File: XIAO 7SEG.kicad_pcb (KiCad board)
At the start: 2 copper layers, 21.1 x 17.8 mm, 8 parts, among them J2 DNP, J4 DNP, Q1 AO3400A, Q2 AO3400A, U1 GS2816CW-G, U2 GS2816CW-G

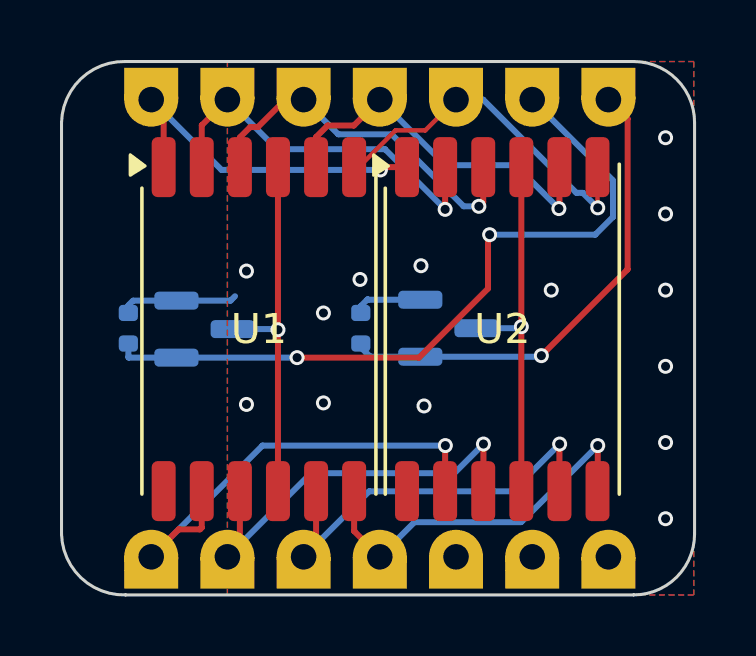
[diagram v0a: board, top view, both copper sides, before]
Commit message: Increase min track/gap to 0.154mm
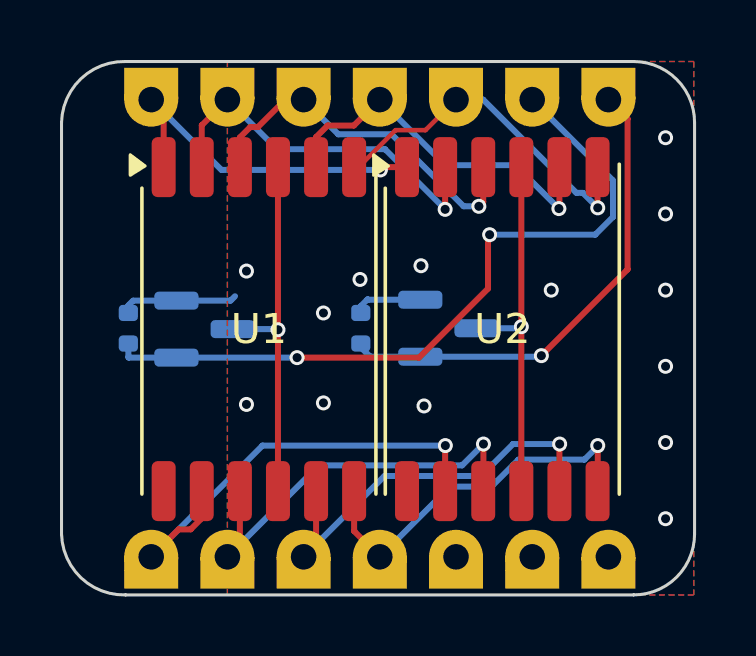
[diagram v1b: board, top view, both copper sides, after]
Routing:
- net SDA: track 12.3 -> 11.7 mm
- net SCK: track 14.0 -> 13.4 mm
- net MISO: track 14.0 -> 13.4 mm
- net TX: track 12.0 -> 11.4 mm
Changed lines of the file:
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@@
 		(title "Xiao_7Seg")
 		(date "2025-08-24")
-		(rev "1")
+		(rev "1.1")
 	)
 	(layers
@@
 	)
 	(segment
-		(start 144.145 109.73)
-		(end 144.145 109.855)
-		(width 0.2)
-		(layer "B.Cu")
-		(net 3)
-	)
-	(segment
 		(start 144.4904 110.17)
 		(end 146.1285 110.17)
@@
 	)
 	(segment
-		(start 142.0368 110.1852)
-		(end 142.022 110.2)
-		(width 0.2)
-		(layer "B.Cu")
-		(net 4)
-	)
-	(segment
 		(start 149.86 101.6)
 		(end 152.5524 104.2924)
@@
 	)
 	(segment
-		(start 145.305502 102.624)
-		(end 146.296 102.624)
-		(width 0.15)
-		(layer "F.Cu")
-		(net 5)
-	)
-	(segment
-		(start 144.079502 103.85)
-		(end 145.305502 102.624)
-		(width 0.15)
+		(start 143.925 103.85)
+		(end 144.071018 103.85)
+		(width 0.154)
 		(layer "F.Cu")
 		(net 5)
 	)
 	(segment
-		(start 143.925 103.85)
-		(end 144.079502 103.85)
-		(width 0.15)
+		(start 144.071018 103.85)
+		(end 145.303018 102.618)
+		(width 0.154)
 		(layer "F.Cu")
 		(net 5)
@@
 		(start 152.0375 103.85)
 		(end 152.0375 105.1999)
-		(width 0.15)
+		(width 0.2)
 		(layer "F.Cu")
 		(net 5)
 	)
 	(segment
-		(start 152.0375 105.1999)
-		(end 152.0444 105.2068)
-		(width 0.15)
+		(start 146.302 102.618)
+		(end 147.32 101.6)
+		(width 0.154)
 		(layer "F.Cu")
 		(net 5)
 	)
 	(segment
-		(start 146.296 102.624)
-		(end 147.32 101.6)
-		(width 0.15)
+		(start 145.303018 102.618)
+		(end 146.302 102.618)
+		(width 0.154)
 		(layer "F.Cu")
 		(net 5)
@@
 	)
 	(segment
-		(start 142.24 101.6)
-		(end 141.6304 101.6)
-		(width 0.2)
-		(layer "F.Cu")
-		(net 6)
-	)
-	(segment
 		(start 140.716 102.5144)
 		(end 140.462 102.5144)
@@
 	)
 	(segment
-		(start 152.0444 114.6431)
-		(end 152.0375 114.65)
-		(width 0.2)
-		(layer "F.Cu")
-		(net 8)
-	)
-	(segment
 		(start 143.925 115.985)
 		(end 144.78 116.84)
@@
 	)
 	(segment
-		(start 144.78 116.84)
-		(end 145.936 115.684)
+		(start 148.5 114.5)
+		(end 149.4 113.6)
+		(width 0.2)
+		(layer "B.Cu")
+		(net 8)
+	)
+	(segment
+		(start 151.6 113.6)
+		(end 152.0444 113.1556)
+		(width 0.2)
+		(layer "B.Cu")
+		(net 8)
+	)
+	(segment
+		(start 147.12 114.5)
+		(end 148.5 114.5)
 		(width 0.2)
 		(layer "B.Cu")
@@
 	)
 	(segment
-		(start 145.936 115.684)
-		(end 149.492 115.684)
+		(start 149.4 113.6)
+		(end 151.6 113.6)
 		(width 0.2)
 		(layer "B.Cu")
@@
 	)
 	(segment
-		(start 149.492 115.684)
+		(start 144.78 116.84)
+		(end 147.12 114.5)
+		(width 0.2)
+		(layer "B.Cu")
+		(net 8)
+	)
+	(segment
+		(start 152.0444 113.1556)
 		(end 152.0444 113.1316)
 		(width 0.2)
@@
 	)
 	(segment
-		(start 137.575 102.015)
-		(end 137.16 101.6)
-		(width 0.2)
-		(layer "F.Cu")
-		(net 10)
-	)
-	(segment
 		(start 137.575 103.85)
 		(end 137.575 102.015)
@@
 	)
 	(segment
-		(start 138.845 115.8662)
-		(end 138.845 114.65)
+		(start 138.4744 115.9256)
+		(end 138.845 115.555)
 		(width 0.2)
 		(layer "F.Cu")
@@
 	)
 	(segment
-		(start 138.7856 115.9256)
-		(end 138.845 115.8662)
+		(start 138.845 115.555)
+		(end 138.845 114.65)
 		(width 0.2)
 		(layer "F.Cu")
@@
 	(segment
 		(start 138.0744 115.9256)
-		(end 138.7856 115.9256)
+		(end 138.4744 115.9256)
 		(width 0.2)
 		(layer "F.Cu")
@@
 		(net 12)
 	)
-	(segment
-		(start 148.2344 114.6431)
-		(end 148.2275 114.65)
-		(width 0.2)
-		(layer "F.Cu")
-		(net 12)
-	)
-	(segment
-		(start 139.7 116.84)
-		(end 140.115 116.425)
-		(width 0.2)
-		(layer "F.Cu")
-		(net 12)
-	)
 	(via
 		(at 148.2344 113.0808)
@@
 	)
 	(segment
-		(start 142.4884 114.0516)
-		(end 147.2636 114.0516)
+		(start 147.5232 113.792)
+		(end 148.2344 113.0808)
 		(width 0.2)
 		(layer "B.Cu")
@@
 	)
 	(segment
-		(start 139.7 116.84)
-		(end 142.4884 114.0516)
+		(start 142.748 113.792)
+		(end 147.5232 113.792)
 		(width 0.2)
 		(layer "B.Cu")
@@
 	)
 	(segment
-		(start 147.2636 114.0516)
-		(end 148.2344 113.0808)
+		(start 139.7 116.84)
+		(end 142.748 113.792)
 		(width 0.2)
 		(layer "B.Cu")
@@
 	)
 	(segment
-		(start 142.24 116.84)
-		(end 142.655 116.425)
-		(width 0.2)
-		(layer "F.Cu")
-		(net 13)
-	)
-	(segment
 		(start 142.655 116.425)
 		(end 142.655 114.65)
@@
 	)
 	(segment
-		(start 149.1996 114.6556)
-		(end 150.7744 113.0808)
+		(start 149.2192 113.0808)
+		(end 148.154 114.146)
+		(width 0.2)
+		(layer "B.Cu")
+		(net 13)
+	)
+	(segment
+		(start 148.154 114.146)
+		(end 144.934 114.146)
 		(width 0.2)
 		(layer "B.Cu")
@@
 	)
 	(segment
-		(start 144.4244 114.6556)
-		(end 149.1996 114.6556)
+		(start 144.934 114.146)
+		(end 142.24 116.84)
 		(width 0.2)
 		(layer "B.Cu")
@@
 	)
 	(segment
-		(start 142.24 116.84)
-		(end 144.4244 114.6556)
+		(start 150.7744 113.0808)
+		(end 149.2192 113.0808)
 		(width 0.2)
 		(layer "B.Cu")

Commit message: V2: Add series resistors
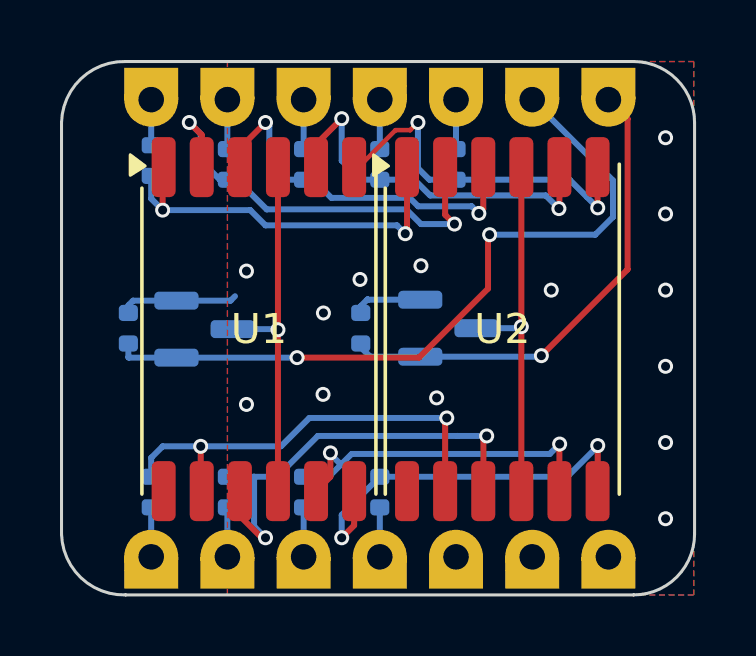
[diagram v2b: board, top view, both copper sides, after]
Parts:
- added R10: 33, Resistor_SMD:R_0402_1005Metric, B.Cu at (142.2, 114.7)
- added R11: 33, Resistor_SMD:R_0402_1005Metric, B.Cu at (144.8, 114.7)
- added R3: 33, Resistor_SMD:R_0402_1005Metric, B.Cu at (147.3, 103.8)
- added R4: 33, Resistor_SMD:R_0402_1005Metric, B.Cu at (144.8, 103.8)
- added R5: 33, Resistor_SMD:R_0402_1005Metric, B.Cu at (142.2, 103.8)
- added R6: 33, Resistor_SMD:R_0402_1005Metric, B.Cu at (139.7, 103.8)
- added R7: 33, Resistor_SMD:R_0402_1005Metric, B.Cu at (137.2, 103.6)
- added R8: 33, Resistor_SMD:R_0402_1005Metric, B.Cu at (137.2, 114.7)
- added R9: 33, Resistor_SMD:R_0402_1005Metric, B.Cu at (139.7, 114.7)
- J2, J4: value DNP -> Conn_01x07
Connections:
- net A0 renamed /LSB_SEL
- net A1 renamed /MSB_SEL
- J2 pad 3: A2 -> /A2
- J2 pad 4: A3 -> /A3
- J2 pad 5: SDA -> /SDA
- J2 pad 6: SCL -> /SCL
- J2 pad 7: TX -> /TX
- J4 pad 1: RX -> /RX
- J4 pad 2: SCK -> /SCK
- J4 pad 3: MISO -> /MISO
- J4 pad 4: MOSI -> /MOSI
- U1 pad 1: TX -> /SEG_G
- U1 pad 10: SCK -> /SEG_D
- U1 pad 11: RX -> /SEG_E
- U1 pad 2: SCL -> /SEG_DP1
- U1 pad 3: SDA -> /SEG_F
- U1 pad 5: A3 -> /SEG_A
- U1 pad 6: A2 -> /SEG_B
- U1 pad 7: MOSI -> /SEG_DP2
- U1 pad 8: MISO -> /SEG_C
- U2 pad 1: TX -> /SEG_G
- U2 pad 10: SCK -> /SEG_D
- U2 pad 11: RX -> /SEG_E
- U2 pad 2: SCL -> /SEG_DP1
- U2 pad 3: SDA -> /SEG_F
- U2 pad 5: A3 -> /SEG_A
- U2 pad 6: A2 -> /SEG_B
- U2 pad 7: MOSI -> /SEG_DP2
- U2 pad 8: MISO -> /SEG_C
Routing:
- net RX: track 16.0 -> 0.00 mm, vias 1 -> 0
- net /SEG_D: track 0.00 -> 15.3 mm, vias 0 -> 2
- net /SEG_E: track 0.00 -> 15.0 mm, vias 0 -> 2
- net /SEG_DP1: track 0.00 -> 14.4 mm, vias 0 -> 2
- net /SEG_DP2: track 0.00 -> 13.5 mm, vias 0 -> 2
- net MISO: track 13.4 -> 0.00 mm, vias 1 -> 0
- net SCK: track 13.4 -> 0.00 mm, vias 1 -> 0
- net /SEG_G: track 0.00 -> 13.4 mm, vias 0 -> 2
- net MOSI: track 12.9 -> 0.00 mm, vias 1 -> 0
- net SCL: track 12.8 -> 0.00 mm, vias 1 -> 0
- net /SEG_A: track 0.00 -> 12.7 mm, vias 0 -> 2
- net /SEG_C: track 0.00 -> 12.6 mm, vias 0 -> 2
- net A3: track 12.5 -> 0.00 mm, vias 1 -> 0
- net /SEG_B: track 0.00 -> 12.0 mm, vias 0 -> 2
- net /SEG_F: track 0.00 -> 12.0 mm, vias 0 -> 2
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
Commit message: Renumber pins to make easier
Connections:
- net /A2 renamed /D2
- net /A3 renamed /D3
- net /LSB_SEL renamed /D0
- net /MISO renamed /D9
- net /MOSI renamed /D10
- net /MSB_SEL renamed /D1
- net /RX renamed /D7
- net /SCK renamed /D8
- net /SCL renamed /D5
- net /SDA renamed /D4
- net /TX renamed /D6
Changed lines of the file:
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@@
 	(net 4 "Net-(Q1-D)")
 	(net 5 "Net-(Q2-D)")
-	(net 6 "/SDA")
-	(net 7 "/MSB_SEL")
-	(net 8 "/A3")
-	(net 9 "/TX")
-	(net 10 "/SCL")
-	(net 11 "/LSB_SEL")
-	(net 12 "/A2")
-	(net 13 "/MISO")
-	(net 14 "/SCK")
-	(net 15 "/MOSI")
-	(net 16 "/RX")
+	(net 6 "/D2")
+	(net 7 "/D1")
+	(net 8 "/D6")
+	(net 9 "/D5")
+	(net 10 "/D3")
+	(net 11 "/D4")
+	(net 12 "/D0")
+	(net 13 "/D7")
+	(net 14 "/D9")
+	(net 15 "/D10")
+	(net 16 "/D8")
 	(net 17 "/SEG_B")
 	(net 18 "/SEG_A")
@@
 			(layers "*.Cu" "*.Mask")
 			(remove_unused_layers no)
-			(net 11 "/LSB_SEL")
+			(net 12 "/D0")
 			(pinfunction "Pin_1")
 			(pintype "passive")
@@
 			(layers "*.Cu" "*.Mask")
 			(remove_unused_layers no)
-			(net 7 "/MSB_SEL")
+			(net 7 "/D1")
 			(pinfunction "Pin_2")
 			(pintype "passive")
@@
 			(layers "*.Cu" "*.Mask")
 			(remove_unused_layers no)
-			(net 12 "/A2")
+			(net 6 "/D2")
 			(pinfunction "Pin_3")
 			(pintype "passive")
@@
 			(layers "*.Cu" "*.Mask")
 			(remove_unused_layers no)
-			(net 8 "/A3")
+			(net 10 "/D3")
 			(pinfunction "Pin_4")
 			(pintype "passive")
@@
 			(layers "*.Cu" "*.Mask")
 			(remove_unused_layers no)
-			(net 6 "/SDA")
+			(net 11 "/D4")
 			(pinfunction "Pin_5")
 			(pintype "passive")
@@
 			(layers "*.Cu" "*.Mask")
 			(remove_unused_layers no)
-			(net 10 "/SCL")
+			(net 9 "/D5")
 			(pinfunction "Pin_6")
 			(pintype "passive")
@@
 			(layers "*.Cu" "*.Mask")
 			(remove_unused_layers no)
-			(net 9 "/TX")
+			(net 8 "/D6")
 			(pinfunction "Pin_7")
 			(pintype "passive")
@@
 			(layers "*.Cu" "*.Mask")
 			(remove_unused_layers no)
-			(net 16 "/RX")
+			(net 13 "/D7")
 			(pinfunction "Pin_1")
 			(pintype "passive")
@@
 			(layers "*.Cu" "*.Mask")
 			(remove_unused_layers no)
-			(net 14 "/SCK")
+			(net 16 "/D8")
 			(pinfunction "Pin_2")
 			(pintype "passive")
@@
 			(layers "*.Cu" "*.Mask")
 			(remove_unused_layers no)
-			(net 13 "/MISO")
+			(net 14 "/D9")
 			(pinfunction "Pin_3")
 			(pintype "passive")
@@
 			(layers "*.Cu" "*.Mask")
 			(remove_unused_layers no)
-			(net 15 "/MOSI")
+			(net 15 "/D10")
 			(pinfunction "Pin_4")
 			(pintype "passive")
@@
 			(layers "B.Cu" "B.Mask" "B.Paste")
 			(roundrect_rratio 0.25)
-			(net 12 "/A2")
+			(net 6 "/D2")
 			(pintype "passive")
 		)
@@
 			(layers "B.Cu" "B.Mask" "B.Paste")
 			(roundrect_rratio 0.25)
-			(net 11 "/LSB_SEL")
+			(net 12 "/D0")
 			(pintype "passive")
 		)
@@
 			(layers "B.Cu" "B.Mask" "B.Paste")
 			(roundrect_rratio 0.25)
-			(net 7 "/MSB_SEL")
+			(net 7 "/D1")
 			(pinfunction "G")
 			(pintype "input")
@@
 			(layers "B.Cu" "B.Mask" "B.Paste")
 			(roundrect_rratio 0.25)
-			(net 7 "/MSB_SEL")
+			(net 7 "/D1")
 			(pintype "passive")
 		)
@@
 			(layers "B.Cu" "B.Mask" "B.Paste")
 			(roundrect_rratio 0.25)
-			(net 11 "/LSB_SEL")
+			(net 12 "/D0")
 			(pinfunction "G")
 			(pintype "input")
@@
 			(layers "B.Cu" "B.Mask" "B.Paste")
 			(roundrect_rratio 0.25)
-			(net 16 "/RX")
+			(net 13 "/D7")
 			(pintype "passive")
 		)
@@
 			(layers "B.Cu" "B.Mask" "B.Paste")
 			(roundrect_rratio 0.25)
-			(net 8 "/A3")
+			(net 10 "/D3")
 			(pintype "passive")
 		)
@@
 			(layers "B.Cu" "B.Mask" "B.Paste")
 			(roundrect_rratio 0.25)
-			(net 9 "/TX")
+			(net 8 "/D6")
 			(pintype "passive")
 		)
@@
 			(layers "B.Cu" "B.Mask" "B.Paste")
 			(roundrect_rratio 0.25)
-			(net 6 "/SDA")
+			(net 11 "/D4")
 			(pintype "passive")
 		)
@@
 			(layers "B.Cu" "B.Mask" "B.Paste")
 			(roundrect_rratio 0.25)
-			(net 13 "/MISO")
+			(net 14 "/D9")
 			(pintype "passive")
 		)
@@
 			(layers "B.Cu" "B.Mask" "B.Paste")
 			(roundrect_rratio 0.25)
-			(net 14 "/SCK")
+			(net 16 "/D8")
 			(pintype "passive")
 		)
@@
 			(layers "B.Cu" "B.Mask" "B.Paste")
 			(roundrect_rratio 0.25)
-			(net 10 "/SCL")
+			(net 9 "/D5")
 			(pintype "passive")
 		)
@@
 			(layers "B.Cu" "B.Mask" "B.Paste")
 			(roundrect_rratio 0.25)
-			(net 15 "/MOSI")
+			(net 15 "/D10")
 			(pintype "passive")
 		)
@@
 	)
 	(segment
-		(start 142.24 103.122)
-		(end 142.24 102.102046)
+		(start 147.32 103.249)
+		(end 147.32 101.6)
 		(width 0.2)
 		(layer "B.Cu")
@@
 	)
 	(segment
-		(start 144.78 101.6)
-		(end 144.78 103.249)
+		(start 137.16 103.122)
+		(end 137.16 101.6)
 		(width 0.2)
 		(layer "B.Cu")
@@
 	)
 	(segment
-		(start 137.16 103.122)
-		(end 137.16 101.6)
+		(start 139.7 103.122)
+		(end 139.7 101.6)
 		(width 0.2)
 		(layer "B.Cu")
@@
 	)
 	(segment
-		(start 139.7 103.122)
-		(end 139.7 101.6)
+		(start 144.78 101.6)
+		(end 144.78 103.249)
 		(width 0.2)
 		(layer "B.Cu")
@@
 	)
 	(segment
+		(start 142.24 103.122)
+		(end 142.24 102.102046)
+		(width 0.2)
+		(layer "B.Cu")
+		(net 11)
+	)
+	(segment
 		(start 150.1648 110.1344)
 		(end 153.039933 107.259267)
 		(width 0.2)
 		(layer "F.Cu")
-		(net 11)
+		(net 12)
 	)
 	(segment
@@
 		(width 0.2)
 		(layer "F.Cu")
-		(net 11)
+		(net 12)
 	)
 	(segment
@@
 		(width 0.2)
 		(layer "F.Cu")
-		(net 11)
+		(net 12)
 	)
 	(via
@@
 		(drill 0.3)
 		(layers "F.Cu" "B.Cu")
-		(net 11)
+		(net 12)
 	)
 	(segment
@@
 		(width 0.2)
 		(layer "B.Cu")
-		(net 11)
+		(net 12)
 	)
 	(segment
@@
 		(width 0.2)
 		(layer "B.Cu")
-		(net 11)
+		(net 12)
 	)
 	(segment
@@
 		(width 0.2)
 		(layer "B.Cu")
-		(net 11)
+		(net 12)
 	)
 	(segment
@@
 		(width 0.2)
 		(layer "B.Cu")
-		(net 11)
+		(net 12)
 	)
 	(segment
@@
 		(width 0.2)
 		(layer "B.Cu")
-		(net 11)
-	)
-	(segment
-		(start 147.32 103.249)
-		(end 147.32 101.6)
-		(width 0.2)
-		(layer "B.Cu")
 		(net 12)
 	)
 	(segment
-		(start 142.24 116.84)
-		(end 142.24 115.191)
+		(start 137.16 116.84)
+		(end 137.16 115.191)
 		(width 0.2)
 		(layer "B.Cu")
@@
 	)
 	(segment
-		(start 139.7 116.84)
-		(end 139.7 115.191)
+		(start 142.24 116.84)
+		(end 142.24 115.191)
 		(width 0.2)
 		(layer "B.Cu")
@@
 	)
 	(segment
-		(start 137.16 116.84)
-		(end 137.16 115.191)
+		(start 139.7 116.84)
+		(end 139.7 115.191)
 		(width 0.2)
 		(layer "B.Cu")

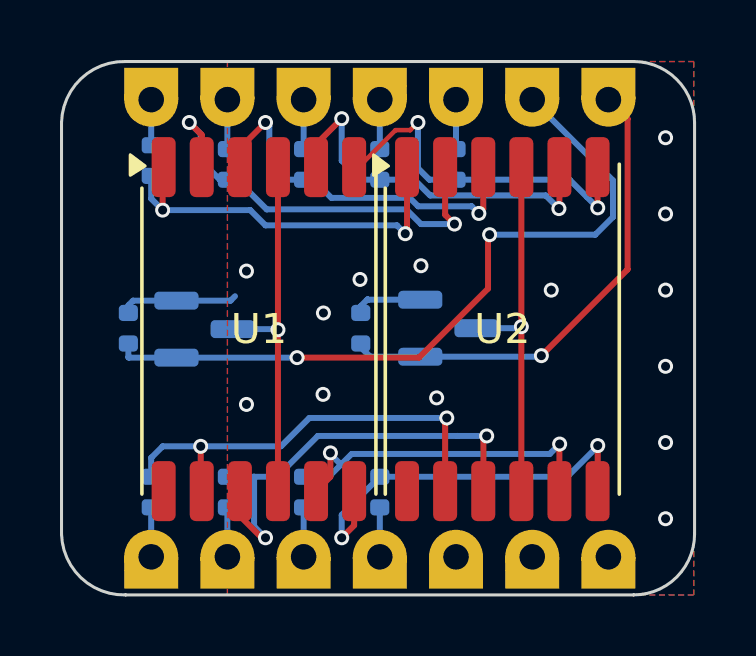
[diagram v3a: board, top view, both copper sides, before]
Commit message: Add supply voltages to silk
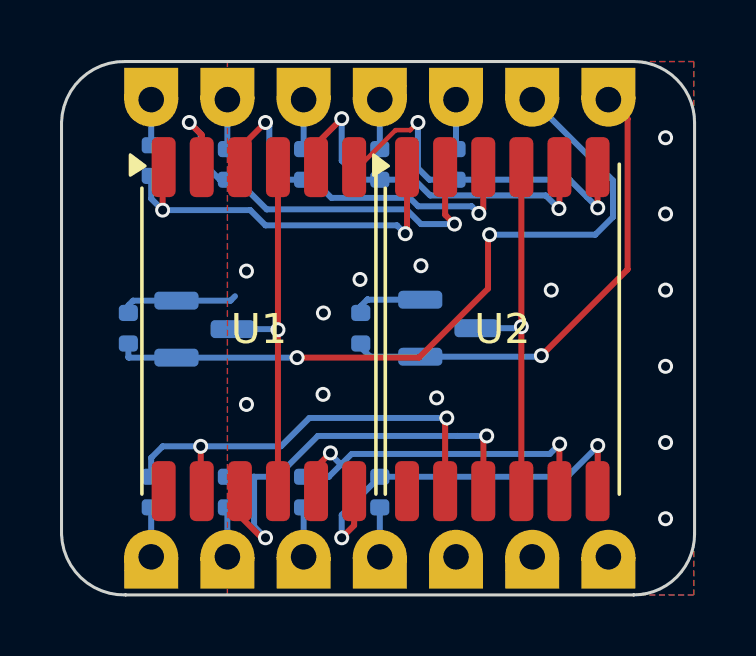
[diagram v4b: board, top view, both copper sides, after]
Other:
- board text added: "3V"
- board text added: "5V"
- board text added: "GND"
- board text added: "REV:${REVISION}"
- board text removed: "242508 V1"
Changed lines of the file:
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@@
 	(title_block
 		(title "Xiao_7Seg")
-		(date "2025-08-24")
-		(rev "2")
+		(date "2025-08-30")
+		(rev "3")
 	)
 	(layers
@@
 			(at -2.413 0 0)
 			(layer "B.SilkS")
+			(hide yes)
 			(effects
 				(font
@@
 			(at 0 2.4 0)
 			(layer "B.SilkS")
+			(hide yes)
 			(effects
 				(font
@@
 			(at -2.413 0 0)
 			(layer "B.SilkS")
+			(hide yes)
 			(effects
 				(font
@@
 			(at 0 2.4 0)
 			(layer "B.SilkS")
+			(hide yes)
 			(effects
 				(font
@@
 		(layer "Edge.Cuts")
 	)
-	(gr_text "242508 V1"
-		(at 154.813 115.57 0)
+	(gr_text "GND\n"
+		(at 149.86 115.316 0)
+		(layer "B.SilkS")
+		(effects
+			(font
+				(size 0.8 0.8)
+				(thickness 0.15)
+			)
+			(justify mirror)
+		)
+	)
+	(gr_text "REV:${REVISION}"
+		(at 144.526 112.649 0)
 		(layer "B.SilkS")
 		(effects
@@
 		)
 	)
+	(gr_text "3V"
+		(at 147.32 115.316 0)
+		(layer "B.SilkS")
+		(effects
+			(font
+				(size 0.8 0.8)
+				(thickness 0.15)
+			)
+			(justify mirror)
+		)
+	)
+	(gr_text "5V"
+		(at 152.4 115.316 0)
+		(layer "B.SilkS")
+		(effects
+			(font
+				(size 0.8 0.8)
+				(thickness 0.15)
+			)
+			(justify mirror)
+		)
+	)
 	(gr_text "USB"
 		(at 156 109.2 -90)
@@
 	)
 	(segment
-		(start 143.132871 114.172129)
-		(end 143.132871 113.376)
+		(start 142.655 114.65)
+		(end 142.655 113.853871)
 		(width 0.2)
 		(layer "F.Cu")
@@
 	)
 	(segment
-		(start 142.655 114.65)
-		(end 143.132871 114.172129)
+		(start 142.655 113.853871)
+		(end 143.132871 113.376)
 		(width 0.2)
 		(layer "F.Cu")
